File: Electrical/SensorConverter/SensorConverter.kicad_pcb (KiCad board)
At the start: 4 copper layers, 77 x 27 mm, 55 parts, among them J1 1990067, J2 0430450600, J3 Conn_ARM_SWD_TagConnect_TC203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, U1 THVD1400DR, U2 LP2950CDTX-3.3/NOPB, U3 STM32F103T8U6, U4 M24M01E-FMC6TG, U5 ISL3176EIUZ, U6 TLA2021IRUGR

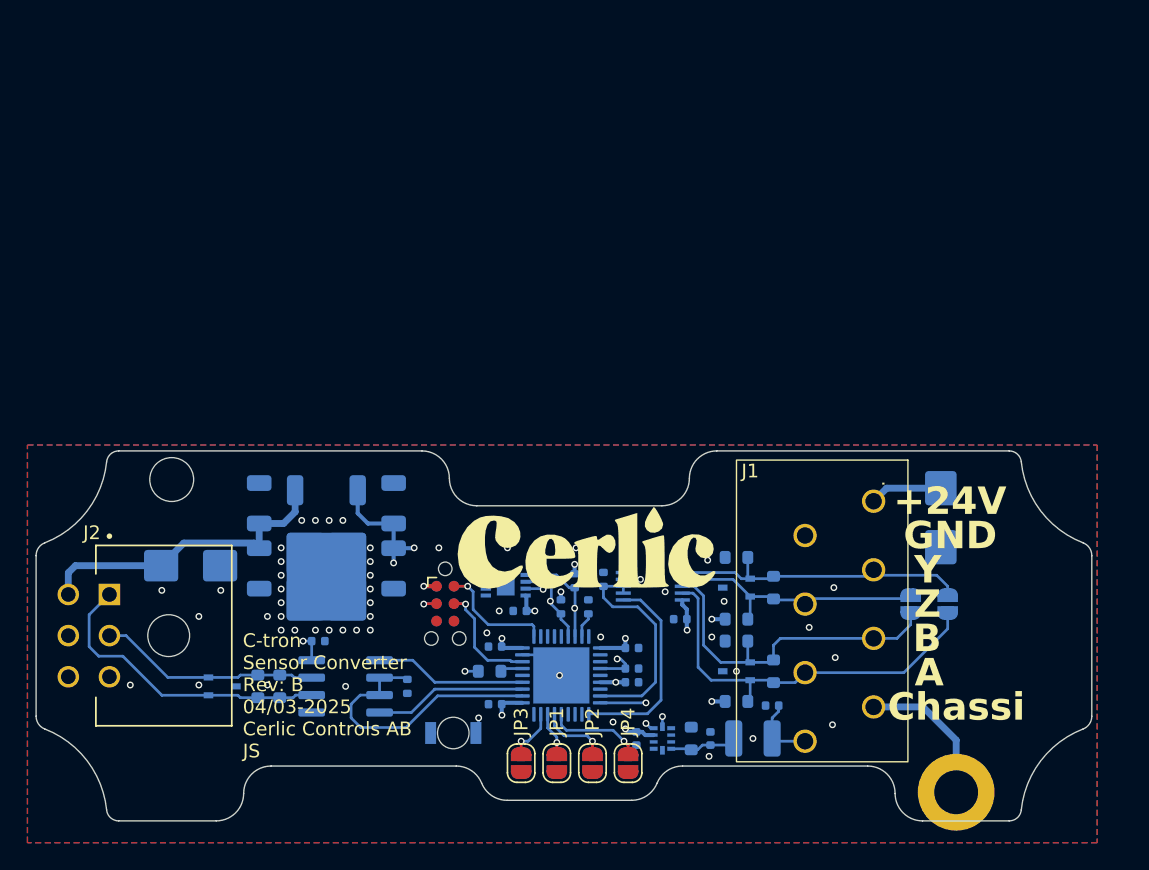
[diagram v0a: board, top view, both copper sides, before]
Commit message: Changing processor to STM32G0
This is mostly because of memory constraints and that the F103 is having a lot of issue.
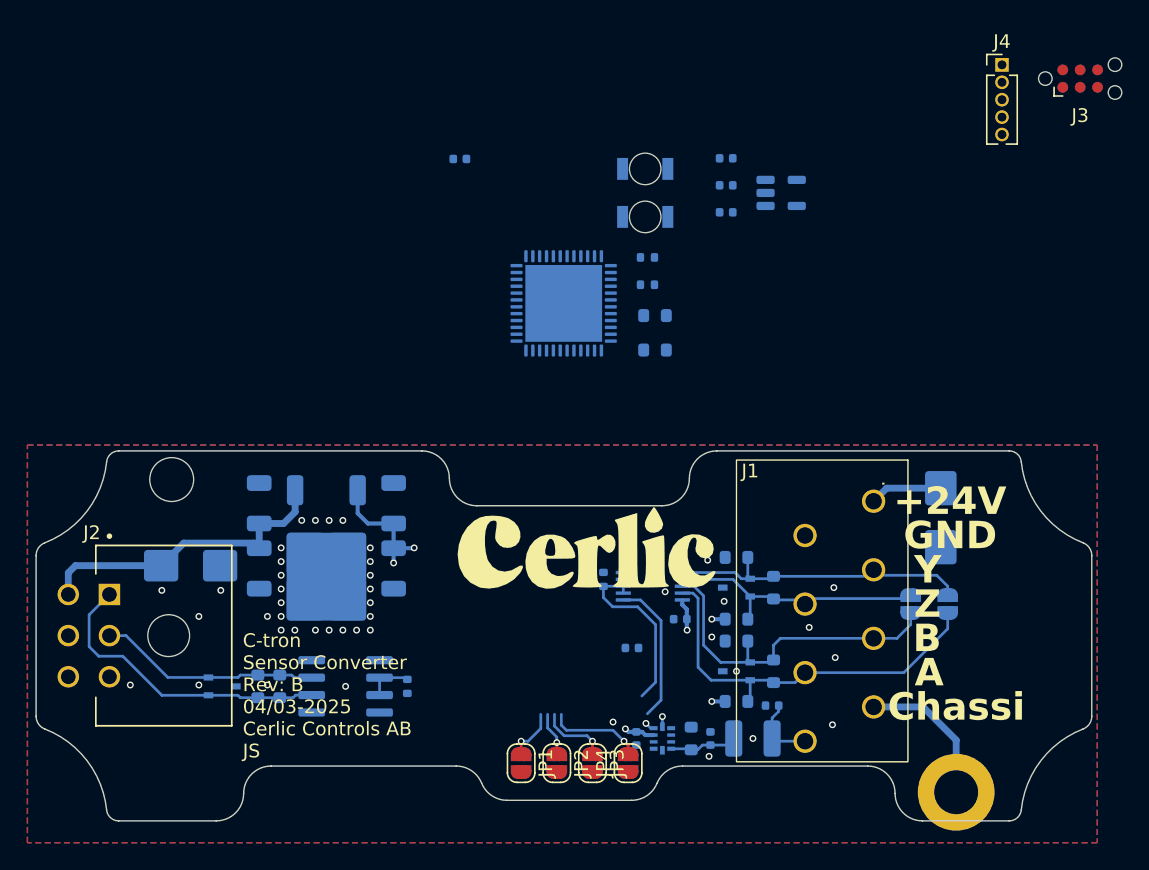
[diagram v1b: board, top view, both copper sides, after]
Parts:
- removed C10, C11, C7, C8, C9: 100nF, Capacitor_SMD:C_0402_1005Metric
- removed R6: 10k, Resistor_SMD:R_0402_1005Metric
- removed U4: M24M01E-FMC6TG, Package_DFN_QFN:DFN-8-1EP_3x2mm_P0.5mm_EP1.3x1.5mm
- added C16: 100nF, Capacitor_SMD:C_0402_1005Metric, B.Cu at (140.9, 63.0)
- added C17: 100nF, Capacitor_SMD:C_0402_1005Metric, B.Cu at (140.9, 61.1)
- added C18: 100nF, Capacitor_SMD:C_0402_1005Metric, B.Cu at (140.9, 59.1)
- added D7: 156120VS75000, LT600_Adapter:WL-SMRW, B.Cu at (135.0, 59.9)
- added J4: Conn_01x05, Connector_PinHeader_1.27mm:PinHeader_1x05_P1.27mm_Vertical, F.Cu at (161.1, 52.3)
- added R16: 768R, Resistor_SMD:R_0603_1608Metric, B.Cu at (135.8, 70.6)
- added U7: STM32G0B1CEUx, Package_DFN_QFN:QFN-48-1EP_7x7mm_P0.5mm_EP5.6x5.6mm, B.Cu at (129.1, 69.7)
- U3: value STM32F103T8U6 -> AT24CS02-STUM; footprint Package_DFN_QFN:QFN-36-1EP_6x6mm_P0.5mm_EP4.1x4.1mm -> Package_TO_SOT_SMD:SOT-23-5
- moved J3 60.1 mm to (166.8, 53.3), turned to 0 degrees
- moved D4 40.1 mm to (135.0, 63.4)
- moved C6 39.2 mm to (121.5, 59.1), turned to 0 degrees
- moved U3 38.7 mm to (145.0, 61.6), turned to 0 degrees
- moved R7 26.3 mm to (135.8, 73.1)
- moved R5 26.2 mm to (135.2, 66.3), turned to 0 degrees
- moved R4 22.2 mm to (135.2, 68.3), turned to 0 degrees
- moved JP3 5.20 mm to (131.2, 103.2), turned to -90 degrees
- moved JP1 2.60 mm to (126.0, 103.2), turned to -90 degrees
- moved JP2 2.60 mm to (128.6, 103.2), turned to -90 degrees
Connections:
- C6 pad 2: RST -> /Processor/RST
- J3 pad 2: SWCLK -> /Processor/SWDIO
- J3 pad 3: RST -> /Processor/RST
- J3 pad 4: SDIO -> /Processor/SWCLK
- JP1 pad 1: GND -> Net-(JP1-A)
- JP1 pad 2: Net-(JP1-B) -> GND
- JP2 pad 1: GND -> Net-(JP2-A)
- JP2 pad 2: Net-(JP2-B) -> GND
- JP3 pad 1: GND -> Net-(JP3-A)
- JP3 pad 2: Net-(JP3-B) -> GND
- R14 pad 2: UART2_DIR -> /Processor/USART2_DE
- R3 pad 1: UART1_DIR -> /Processor/USART1_DE
- R4 pad 2: SDA -> /4-20mA/SDA
- R5 pad 2: SCL -> /4-20mA/SCL
- R7 pad 2: Net-(U3-PA12) -> Net-(U7-PB13)
- U1 pad 1: UART1_RX -> /Processor/USART1_RX
- U1 pad 2: UART1_DIR -> /Processor/USART1_DE
- U1 pad 3: UART1_DIR -> /Processor/USART1_DE
- U1 pad 4: UART1_TX -> /Processor/USART1_TX
- U3 pad 1: +3V3 -> /4-20mA/SCL
- U3 pad 2: unconnected-(U3-PD0-Pad2) -> GND
- U3 pad 3: unconnected-(U3-PD1-Pad3) -> /4-20mA/SDA
- U3 pad 4: RST -> +3V3
- U5 pad 1: UART2_RX -> /Processor/USART2_RX
- U5 pad 2: UART2_DIR -> /Processor/USART2_DE
- U5 pad 3: UART2_DIR -> /Processor/USART2_DE
- U5 pad 4: UART2_TX -> /Processor/USART2_TX
- U6 pad 10: SCL -> /4-20mA/SCL
- U6 pad 9: SDA -> /4-20mA/SDA
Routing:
- net SCL: track 22.7 -> 0.00 mm, vias 2 -> 0
- net SDA: track 20.9 -> 0.00 mm, vias 2 -> 0
- net UART1_DIR: track 20.4 -> 0.00 mm
- net RST: track 20.4 -> 0.00 mm, vias 2 -> 0
- net UART2_DIR: track 16.0 -> 0.00 mm
- net +3V3: track 30.5 -> 15.5 mm, vias 16 -> 7
- net UART2_RX: track 14.9 -> 0.00 mm
- net UART2_TX: track 14.7 -> 0.00 mm, vias 2 -> 0
- net /Processor/USART2_DE: track 0.00 -> 13.0 mm
- net UART1_TX: track 11.1 -> 0.00 mm
- net UART1_RX: track 11.1 -> 0.00 mm
- net /Processor/USART2_RX: track 0.00 -> 10.6 mm
- net SWCLK: track 8.54 -> 0.00 mm, vias 1 -> 0
- net SDIO: track 8.21 -> 0.00 mm, vias 1 -> 0
- net Net-(D4-A): track 6.09 -> 0.00 mm, vias 2 -> 0
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
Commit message: Finalized PCB RevB
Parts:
- removed C18: 100nF, Capacitor_SMD:C_0402_1005Metric
- moved J4 67.2 mm to (115.8, 101.9), turned to -90 degrees
- moved J3 66.5 mm to (120.6, 101.2)
- moved D7 42.5 mm to (163.8, 91.1), turned to 180 degrees
- moved D4 42.3 mm to (163.8, 94.4), turned to 180 degrees
- moved U3 36.8 mm to (135.3, 97.1), turned to 90 degrees
- moved R7 33.0 mm to (160.2, 95.2), turned to -90 degrees
- moved C17 32.2 mm to (125.0, 89.0), turned to -90 degrees
- moved C16 31.8 mm to (135.4, 94.4), turned to 180 degrees
- moved R5 31.5 mm to (137.7, 97.7), turned to -90 degrees
- moved R16 31.4 mm to (160.2, 90.3), turned to 90 degrees
- moved C6 30.3 mm to (126.5, 89.0), turned to -90 degrees
- moved R4 29.5 mm to (133.0, 97.7), turned to -90 degrees
- moved U7 25.1 mm to (125.7, 94.5), turned to -90 degrees
- moved C5 23.0 mm to (111.1, 94.3)
- moved JP1 7.80 mm to (133.8, 103.2)
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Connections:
- J4 pad 3: /Processor/SWCLK -> /Processor/SWDIO
- J4 pad 4: /Processor/SWDIO -> /Processor/SWCLK
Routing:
- net Net-(U7-PB14): track 0.00 -> 43.9 mm, vias 0 -> 2
- net Net-(U7-PB13): track 0.00 -> 38.2 mm, vias 0 -> 2
- net /Processor/RST: track 0.00 -> 28.9 mm, vias 0 -> 1
- net /4-20mA/SCL: track 0.81 -> 19.0 mm, vias 1 -> 2
- net /Processor/SWCLK: track 0.00 -> 15.0 mm, vias 0 -> 1
- net /Processor/USART1_TX: track 0.00 -> 14.8 mm
- net /Processor/SWDIO: track 0.00 -> 14.5 mm, vias 0 -> 1
- net +3V3: track 15.5 -> 28.0 mm, vias 7 -> 11
- net /4-20mA/SDA: track 0.71 -> 12.4 mm, vias 1 -> 2
- net /Processor/USART1_DE: track 3.35 -> 11.5 mm, vias 0 -> 2
- net /Processor/USART1_RX: track 0.00 -> 7.93 mm
- net /Processor/USART2_TX: track 0.00 -> 7.22 mm, vias 0 -> 2
- net /Processor/USART2_DE: track 13.0 -> 6.12 mm
- net Net-(JP1-A): track 3.80 -> 10.1 mm
- net /Processor/USART2_RX: track 10.6 -> 4.71 mm
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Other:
- board text added: "C-tron Sensor Converter Rev: B 02/04-2025 Cerlic Controls AB JS"
- board text removed: "C-tron Sensor Converter Rev: B 04/03-2025 Cerlic Controls AB JS"

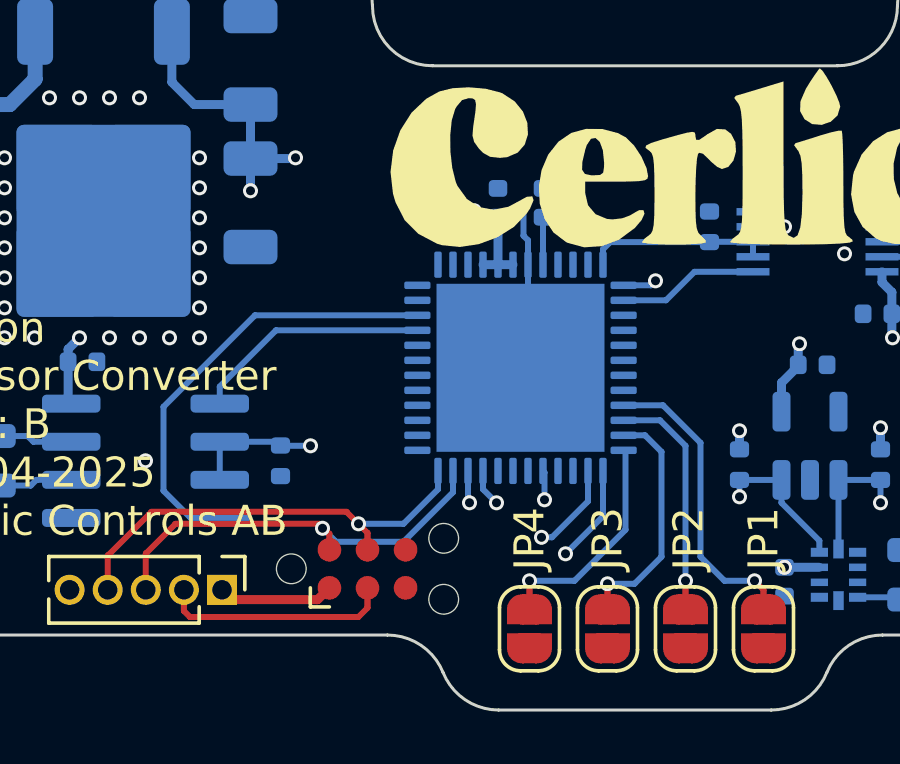
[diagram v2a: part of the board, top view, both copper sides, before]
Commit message: Fixed minor changes in PCB
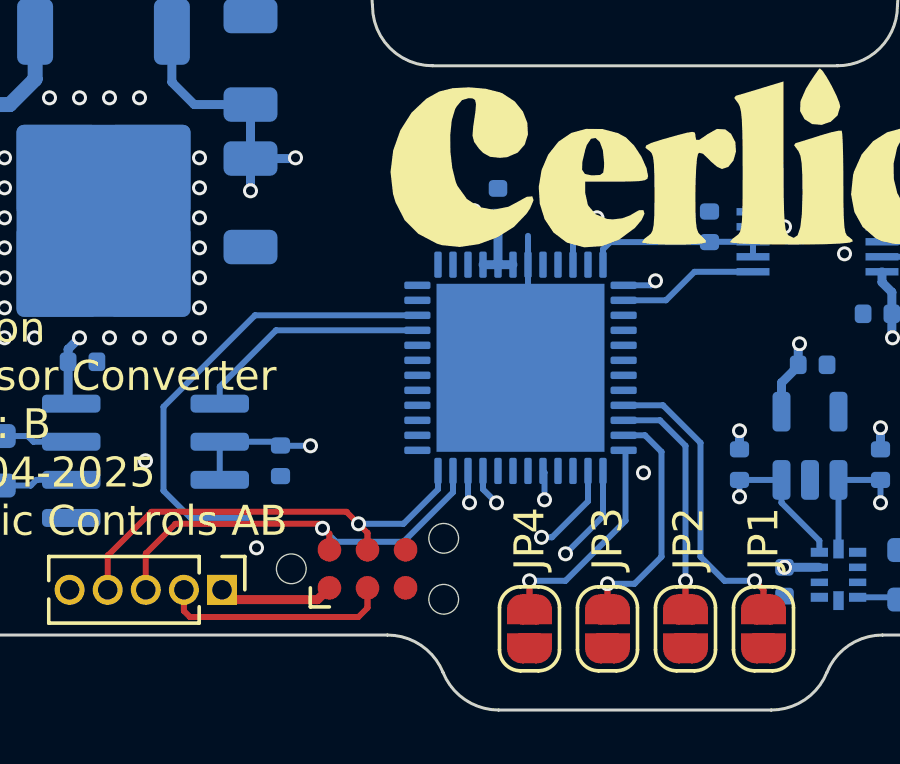
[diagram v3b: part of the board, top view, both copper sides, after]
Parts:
- moved C6 1.00 mm to (127.5, 89.0)
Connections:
- U7 pad 10: unconnected-(U7-PF2-Pad10) -> /Processor/RST
- U7 pad 8: /Processor/RST -> unconnected-(U7-PF0-Pad8)
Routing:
- net /Processor/RST: track 28.9 -> 30.0 mm
- net GND: track 5.61 -> 4.50 mm, vias 41 -> 43
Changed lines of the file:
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@@
 	(net 20 "Net-(U7-PB14)")
 	(net 21 "/Processor/USART2_TX")
-	(net 22 "unconnected-(U7-PF2-Pad10)")
+	(net 22 "unconnected-(U7-PF0-Pad8)")
 	(net 23 "/Processor/USART2_DE")
 	(net 24 "unconnected-(U7-PC6-Pad30)")
@@
 			(layers "B.Cu" "B.Mask" "B.Paste")
 			(roundrect_rratio 0.25)
-			(net 9 "/Processor/RST")
+			(net 22 "unconnected-(U7-PF0-Pad8)")
 			(pinfunction "PF0")
 			(pintype "bidirectional")
@@
 			(layers "B.Cu" "B.Mask" "B.Paste")
 			(roundrect_rratio 0.25)
-			(net 22 "unconnected-(U7-PF2-Pad10)")
+			(net 9 "/Processor/RST")
 			(pinfunction "PF2")
 			(pintype "bidirectional")
@@
 	(footprint "Capacitor_SMD:C_0402_1005Metric"
 		(layer "B.Cu")
-		(at 126.45 89 -90)
+		(at 127.45 89 -90)
 		(descr "Capacitor SMD 0402 (1005 Metric), square (rectangular) end terminal, IPC_7351 nominal, (Body size source: IPC-SM-782 page 76, https://www.pcb-3d.com/wordpress/wp-content/uploads/ipc-sm-782a_amendment_1_and_2.pdf), generated with kicad-footprint-generator")
 		(tags "capacitor")
@@
 	)
 	(via
+		(at 129.8 98)
+		(size 0.5)
+		(drill 0.3)
+		(layers "F.Cu" "B.Cu")
+		(free yes)
+		(net 2)
+	)
+	(via
 		(at 108.5 91.5)
 		(size 0.5)
@@
 	)
 	(via
+		(at 116.9 100.5)
+		(size 0.5)
+		(drill 0.3)
+		(layers "F.Cu" "B.Cu")
+		(free yes)
+		(net 2)
+	)
+	(via
 		(at 113 85.5)
 		(size 0.5)
@@
 	)
 	(segment
-		(start 125.8 90.1)
-		(end 125.8 89.2)
-		(width 0.2)
-		(layer "B.Cu")
-		(net 2)
-	)
-	(segment
-		(start 125.8 89.2)
-		(end 125.7 89.1)
-		(width 0.2)
-		(layer "B.Cu")
-		(net 2)
-	)
-	(segment
 		(start 125.95 91.0625)
 		(end 125.95 94.25)
@@
 	)
 	(segment
-		(start 125.95 91.0625)
-		(end 125.95 90.25)
-		(width 0.2)
-		(layer "B.Cu")
-		(net 2)
-	)
-	(segment
-		(start 125.95 90.25)
-		(end 125.8 90.1)
+		(start 125.95 94.25)
+		(end 125.7 94.5)
 		(width 0.2)
 		(layer "B.Cu")
@@
 	)
 	(segment
-		(start 125.95 94.25)
-		(end 125.7 94.5)
+		(start 125.95 91.0625)
+		(end 125.95 90.1)
 		(width 0.2)
 		(layer "B.Cu")
@@
 	)
 	(via
-		(at 127.2 89.5)
+		(at 128.25 89.5)
 		(size 0.5)
 		(drill 0.3)
@@
 	)
 	(segment
-		(start 126.47 89.5)
-		(end 126.45 89.48)
+		(start 127.45 89.48)
+		(end 127.5 89.48)
 		(width 0.2)
 		(layer "B.Cu")
@@
 	)
 	(segment
-		(start 126.45 89.48)
-		(end 126.45 91.0625)
+		(start 127.45 89.48)
+		(end 127.45 91.0625)
 		(width 0.2)
 		(layer "B.Cu")
@@
 	)
 	(segment
-		(start 127.2 89.5)
-		(end 126.47 89.5)
+		(start 127.47 89.5)
+		(end 127.45 89.48)
 		(width 0.2)
 		(layer "B.Cu")
@@
 	)
 	(segment
-		(start 125.2 89.5)
-		(end 127.2 89.5)
+		(start 128.25 89.5)
+		(end 127.47 89.5)
 		(width 0.2)
-		(layer "In1.Cu")
+		(layer "B.Cu")
 		(net 9)
 	)
 	(segment
-		(start 114.48 101.9)
+		(start 125.2 89.5)
 		(end 114.48 100.22)
 		(width 0.2)
@@
 	(segment
 		(start 114.48 100.22)
+		(end 114.48 101.9)
+		(width 0.2)
+		(layer "In1.Cu")
+		(net 9)
+	)
+	(segment
+		(start 128.25 89.5)
 		(end 125.2 89.5)
 		(width 0.2)
@@
 	)
 	(segment
-		(start 129.2 97.3125)
-		(end 129.1375 97.25)
+		(start 129.2 99.6)
+		(end 129.2 97.3125)
 		(width 0.2)
 		(layer "B.Cu")
@@
 	)
 	(segment
-		(start 129.2 99.9)
-		(end 129.2 97.3125)
+		(start 129.2 97.3125)
+		(end 129.1375 97.25)
 		(width 0.2)
 		(layer "B.Cu")
@@
 	)
 	(segment
-		(start 126 101.6)
-		(end 127.5 101.6)
+		(start 127.2 101.6)
+		(end 129.2 99.6)
 		(width 0.2)
 		(layer "B.Cu")
@@
 	)
 	(segment
-		(start 127.5 101.6)
-		(end 129.2 99.9)
+		(start 126 101.6)
+		(end 127.2 101.6)
 		(width 0.2)
 		(layer "B.Cu")

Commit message: WIP
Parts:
- removed J4: Conn_01x05, Connector_PinHeader_1.27mm:PinHeader_1x05_P1.27mm_Vertical
- U3: value AT24CS02-STUM -> 24CS256T-I/OT
- moved J3 0.51 mm to (121.1, 101.3), turned to 180 degrees
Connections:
- U7 pad 29: /4-20mA/SDA -> /Processor/USART1_TX
- U7 pad 32: unconnected-(U7-PA10/UCPD1_DBCC2-Pad32) -> /Processor/USART1_RX
- U7 pad 33: /4-20mA/SCL -> unconnected-(U7-PA9/PA11-Pad33)
- U7 pad 45: /Processor/USART1_RX -> /4-20mA/SCL
- U7 pad 46: /Processor/USART1_TX -> /4-20mA/SDA
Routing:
- net /Processor/USART1_RX: track 7.93 -> 17.7 mm, vias 0 -> 2
- net /Processor/SWCLK: track 15.0 -> 6.26 mm
- net /Processor/SWDIO: track 14.5 -> 5.83 mm
- net /4-20mA/SDA: track 12.4 -> 20.9 mm
- net /4-20mA/SCL: track 19.0 -> 27.1 mm
- net /Processor/USART1_DE: track 11.5 -> 19.0 mm
- net /Processor/RST: track 30.0 -> 22.9 mm, vias 1 -> 2
- net +3V3: track 28.0 -> 26.4 mm, vias 11 -> 12
- net /Processor/USART1_TX: track 14.8 -> 15.2 mm, vias 0 -> 2
- net GND: vias 43 -> 44
